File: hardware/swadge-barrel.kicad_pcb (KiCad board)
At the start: 2 copper layers, 70.4 x 89.6 mm, 45 parts, among them J1 USB_B_Micro, Q1 Q_NPN_BEC, SW2 4-1437565-2, SW4 SW_SPDT, U1 ESP-13-WROOM-02D, U2 DISP_OLED_UG-2864HSWEG01, U3 BUS_PCIexpress, U4 QMA6981, U5 AP1117-33

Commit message: Routed board and lots of other things
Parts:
- moved R6 30.9 mm to (165.1, 85.8)
- moved C4 28.9 mm to (159.9, 96.5)
- moved C9 28.8 mm to (131.1, 96.5), turned to 90 degrees
- moved R7 18.1 mm to (134.2, 69.0)
- moved R4 14.2 mm to (172.2, 64.2), turned to 178 degrees
- moved R5 14.0 mm to (172.1, 68.4), turned to 178 degrees
- moved Q1 13.8 mm to (130.5, 69.0), turned to 270 degrees
- moved R3 10.1 mm to (168.3, 64.1), turned to 178 degrees
- moved R2 9.96 mm to (168.2, 68.3), turned to 178 degrees
- moved C2 9.82 mm to (142.8, 61.7), turned to 268 degrees
- moved U1 9.80 mm to (146.3, 60.5), turned to 358 degrees
- moved C3 9.71 mm to (142.7, 64.7), turned to 88 degrees
- moved R1 9.60 mm to (142.6, 67.8), turned to 268 degrees
- moved C1 9.50 mm to (142.5, 70.8), turned to 88 degrees
- moved BZ1 8.70 mm to (136.2, 60.2)
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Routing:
- net +3V3: track 250.7 -> 317.7 mm, vias 7 -> 8
- net GND: track 12.7 -> 64.0 mm, vias 11 -> 16
- net SDA: track 119.7 -> 143.7 mm, vias 5 -> 8
- net _RES: track 105.1 -> 125.7 mm, vias 4 -> 7
- net Net-(R6-Pad2): track 0.00 -> 20.4 mm
- net Net-(C9-Pad1): track 0.00 -> 20.1 mm
- net SCL: track 112.8 -> 131.5 mm, vias 5 -> 8
- net Net-(C9-Pad2): track 0.00 -> 17.6 mm
- net Net-(C7-Pad2): track 0.00 -> 16.0 mm
- net Net-(C5-Pad1): track 0.00 -> 15.3 mm
- net Net-(C5-Pad2): track 0.00 -> 15.1 mm
- net Net-(C10-Pad2): track 0.00 -> 12.4 mm
- net SW5: track 118.4 -> 107.8 mm
- net RX: track 80.1 -> 88.6 mm
- net SW2: track 111.5 -> 117.3 mm
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
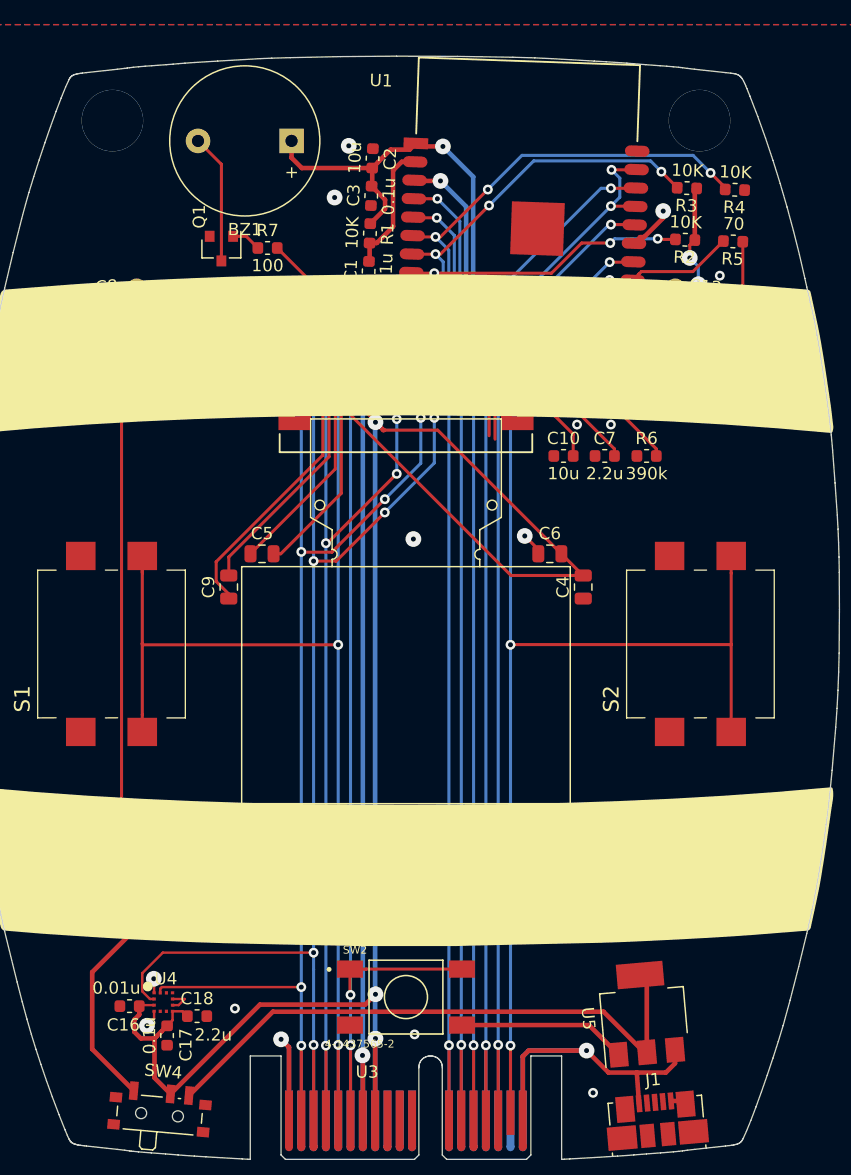
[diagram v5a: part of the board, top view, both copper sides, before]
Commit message: Now has a single hole
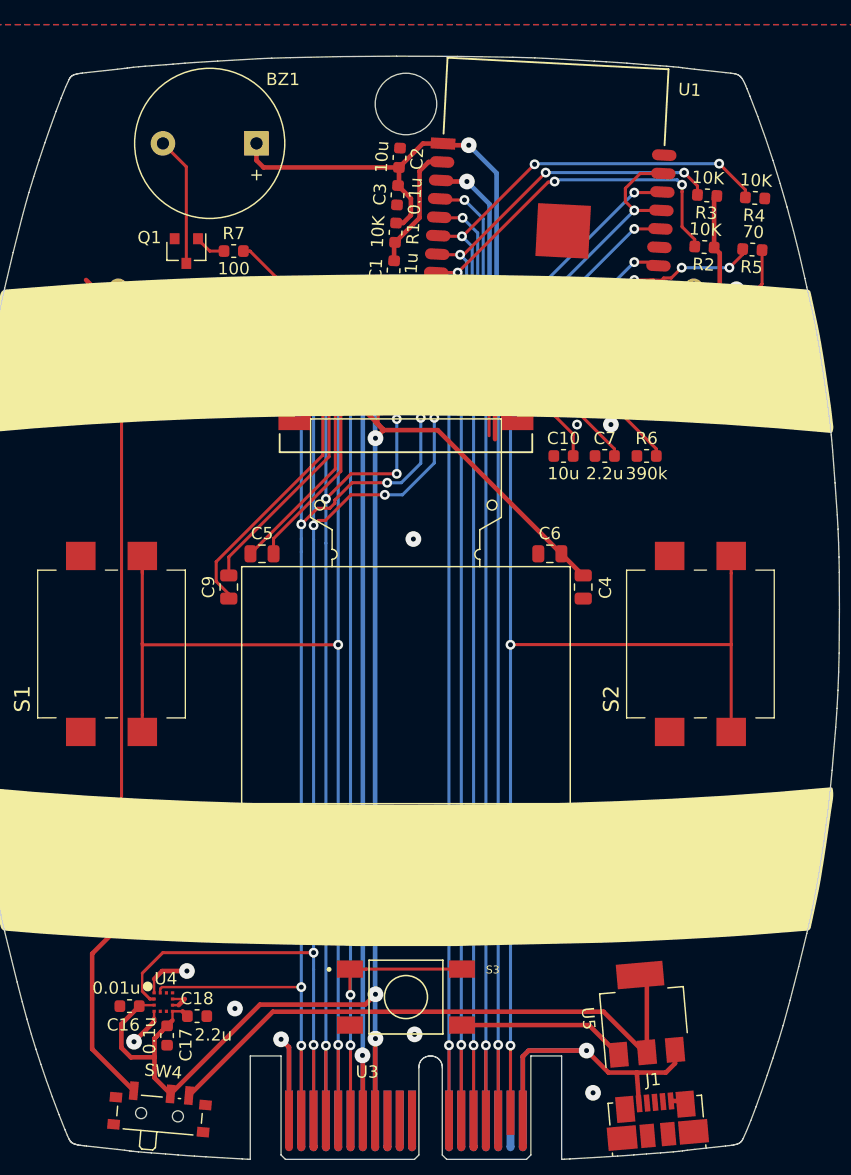
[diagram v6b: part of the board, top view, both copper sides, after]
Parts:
- moved BZ1 2.86 mm to (133.3, 60.5)
- moved Q1 2.86 mm to (127.7, 69.2)
- moved R7 2.76 mm to (131.5, 69.2)
- moved U1 2.21 mm to (148.5, 60.5), turned to 357 degrees
- moved C2 2.19 mm to (145.0, 61.6), turned to 267 degrees
- moved C3 2.14 mm to (144.8, 64.7), turned to 87 degrees
- moved R1 2.08 mm to (144.7, 67.7), turned to 267 degrees
- moved C1 2.03 mm to (144.5, 70.8), turned to 87 degrees
- moved R4 1.77 mm to (173.9, 64.9), turned to 177 degrees
- moved R3 1.75 mm to (170.0, 64.7), turned to 177 degrees
- moved R5 1.70 mm to (173.6, 69.1), turned to 177 degrees
- moved R2 1.68 mm to (169.7, 68.9), turned to 177 degrees
- moved BT1 1.50 mm to (168.9, 98.2)
- moved BT2 1.50 mm to (122.1, 98.2)
- moved D1 0.75 mm to (167.4, 77.7)
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- renumbered SW2 to S3
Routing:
- net +3V3: track 317.7 -> 304.4 mm, vias 8 -> 6
- net SCL: track 131.5 -> 138.8 mm
- net SW5: track 107.8 -> 113.7 mm
- net GND: track 64.0 -> 69.7 mm, vias 16 -> 12
- net Net-(BT1-Pad1): track 45.3 -> 49.7 mm
- net SW2: track 117.3 -> 119.1 mm
- net SW3: track 98.3 -> 100.1 mm
- net AUD_PWR: track 87.9 -> 89.6 mm
- net TX: track 81.7 -> 82.7 mm
- net SW4: track 109.6 -> 110.5 mm
- net Net-(D3-Pad2): track 42.6 -> 41.8 mm
- net REST: track 92.8 -> 93.5 mm, vias 3 -> 2
- net Net-(D1-Pad4): track 8.30 -> 9.02 mm
- net Net-(BT2-Pad1): track 16.1 -> 15.5 mm
- net RX: track 88.6 -> 89.1 mm, vias 2 -> 4
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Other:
- outline, holes or cut-outs redrawn

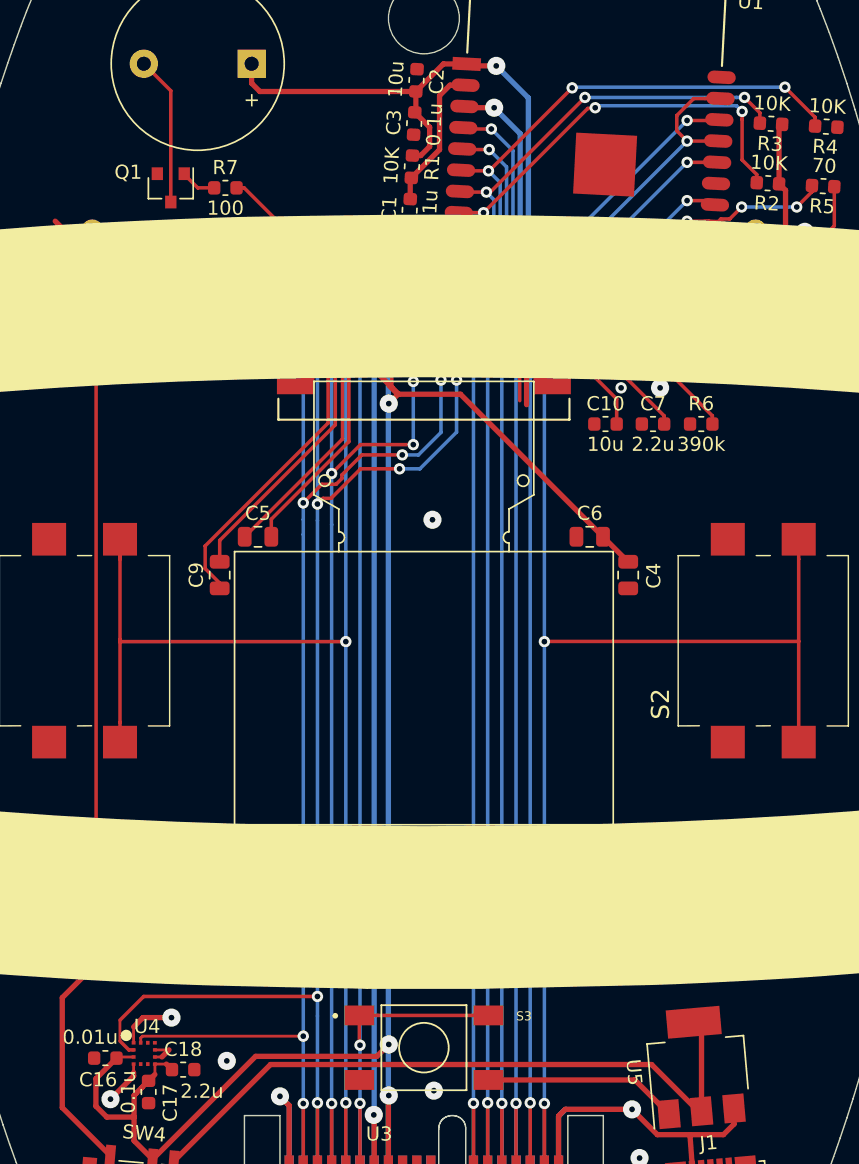
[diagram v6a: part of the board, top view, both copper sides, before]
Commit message: fixed all DRC errors
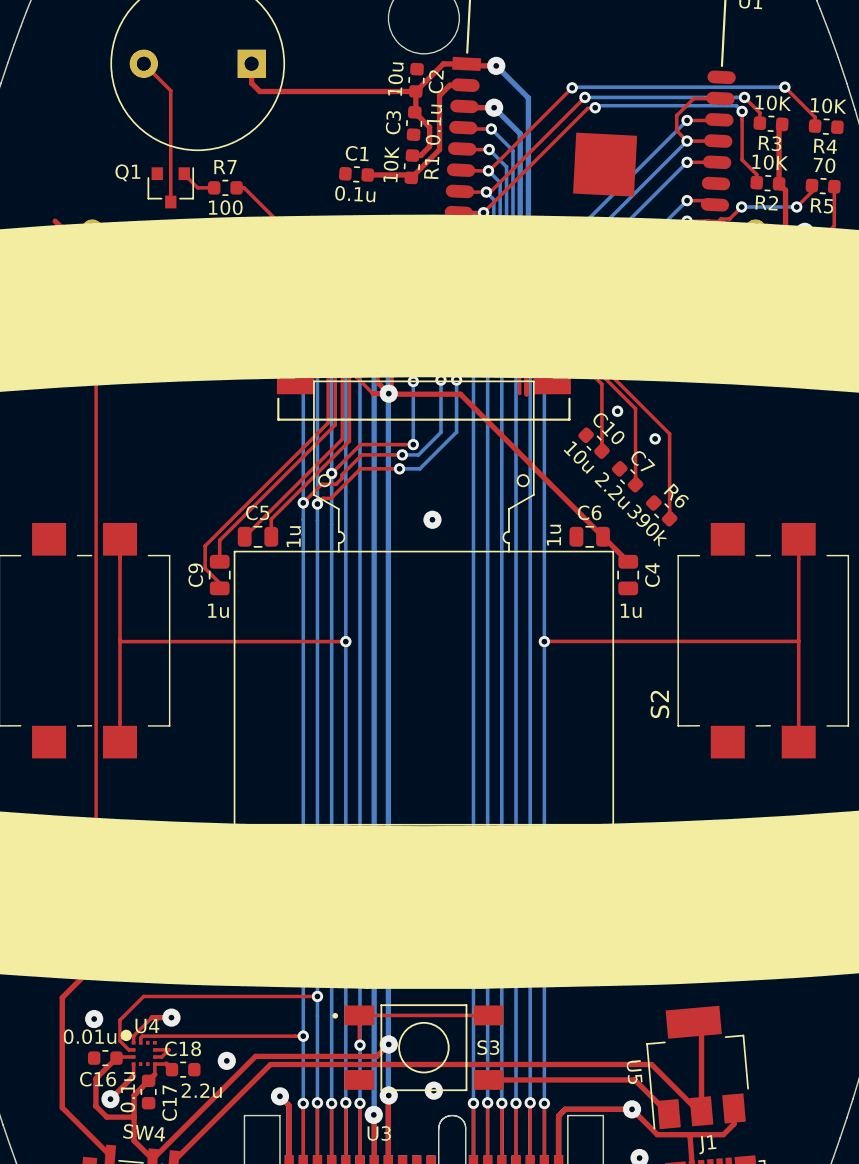
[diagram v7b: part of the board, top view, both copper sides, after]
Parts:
- moved R6 6.73 mm to (162.3, 92.0), turned to 315 degrees
- moved C1 4.52 mm to (140.8, 68.2), turned to 357 degrees
- moved C7 4.13 mm to (159.9, 89.6), turned to 315 degrees
- moved C10 1.57 mm to (157.5, 87.2), turned to 315 degrees
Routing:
- net Net-(R6-Pad2): track 20.4 -> 23.3 mm
- net Net-(C7-Pad2): track 16.0 -> 18.6 mm
- net Net-(C1-Pad2): track 10.3 -> 12.0 mm
- net Net-(C10-Pad2): track 12.4 -> 13.9 mm
- net +3V3: track 304.4 -> 305.1 mm
- net GND: track 69.7 -> 69.4 mm, vias 12 -> 13

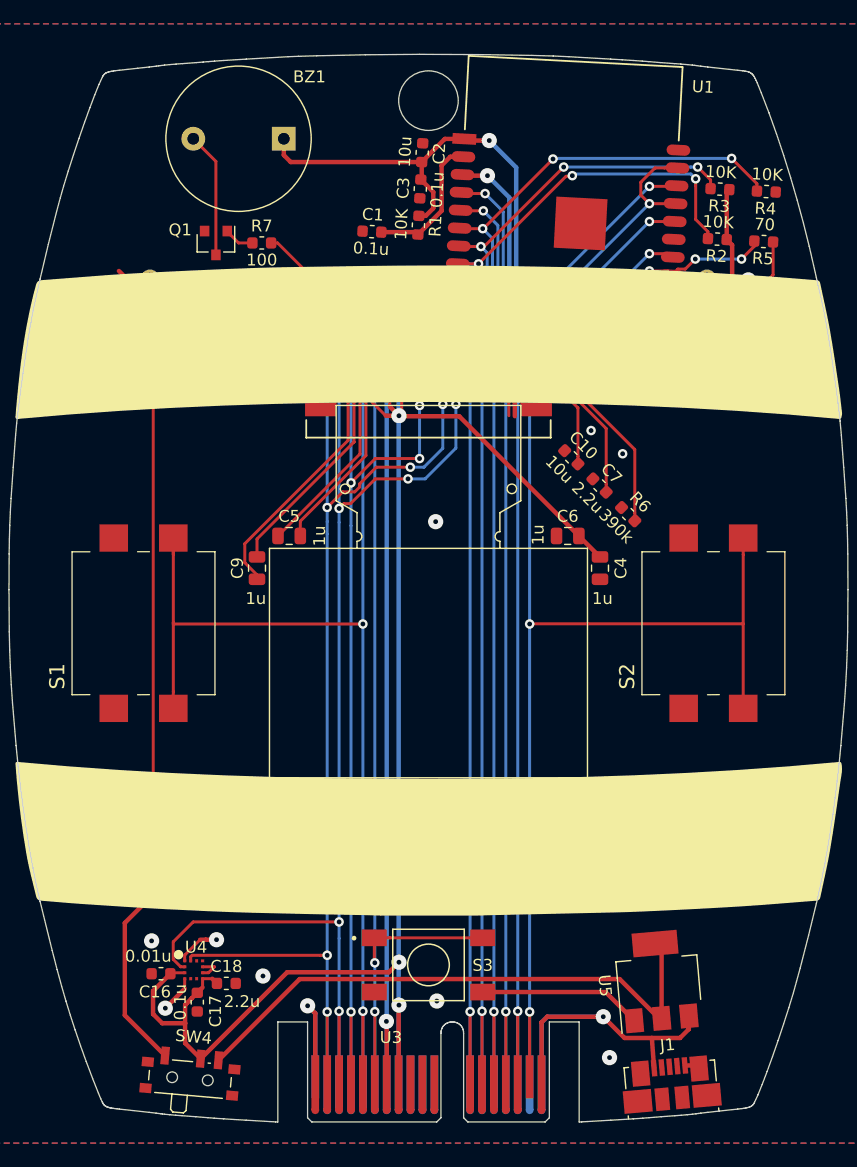
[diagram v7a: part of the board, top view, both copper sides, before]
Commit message: Moved a lot of silk to F.Fab. Updated buzzer footprint
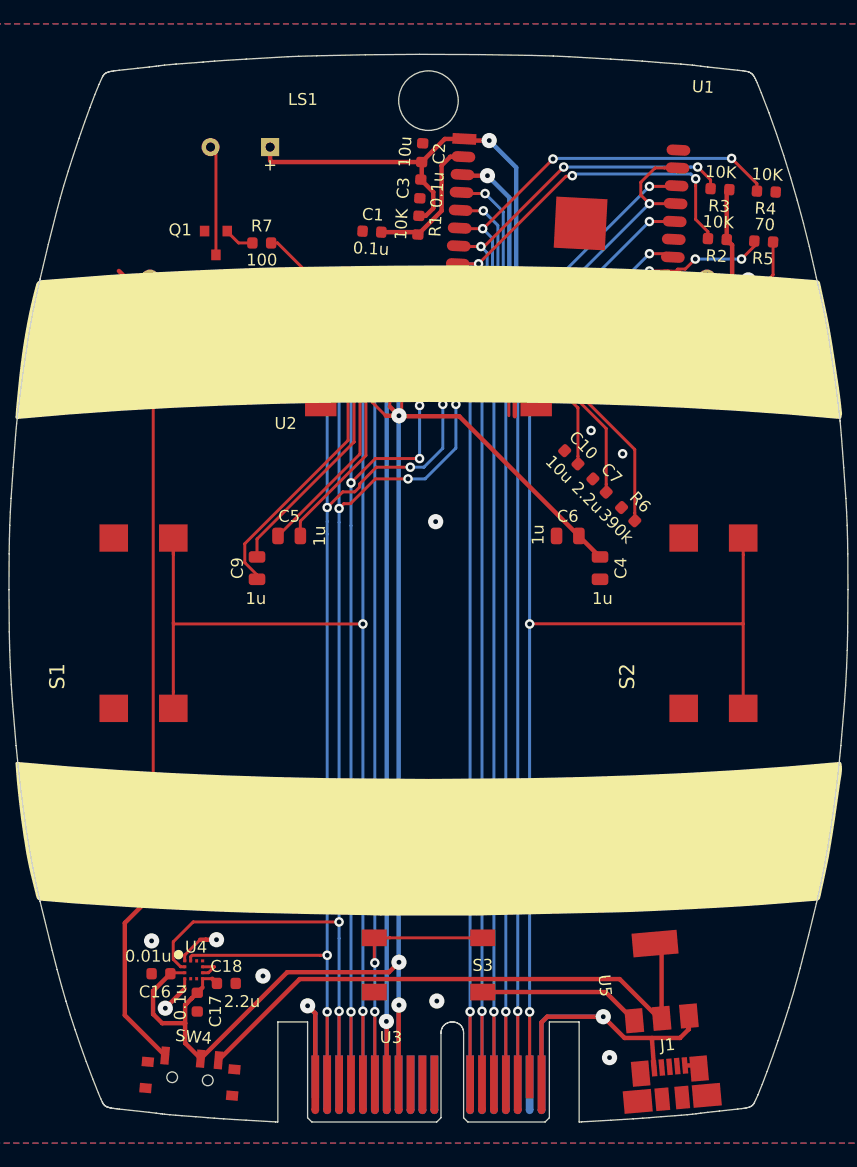
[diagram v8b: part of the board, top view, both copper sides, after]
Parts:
- removed BZ1: Buzzer, Swadge_Parts:Buzzer_12x9.5RM7.6
- added LS1: Speaker, Swadge_Parts:Speaker_9mm, F.Cu at (129.7, 61.1)
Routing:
- net Net-(LS1-Pad2): track 10.5 -> 9.24 mm
- net +3V3: track 305.1 -> 305.8 mm
